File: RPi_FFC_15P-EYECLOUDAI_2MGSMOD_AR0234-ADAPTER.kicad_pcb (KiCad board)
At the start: 2 copper layers, 40.4 x 40.5 mm, 21 parts, among them J1 1-84952-5, J2 3-1734592-0, P1 53261-0371, P2 53261-0371, U1 MIC5259-1.8YD5-TR, U2 APX803-29SAG-7, X1 24MHz

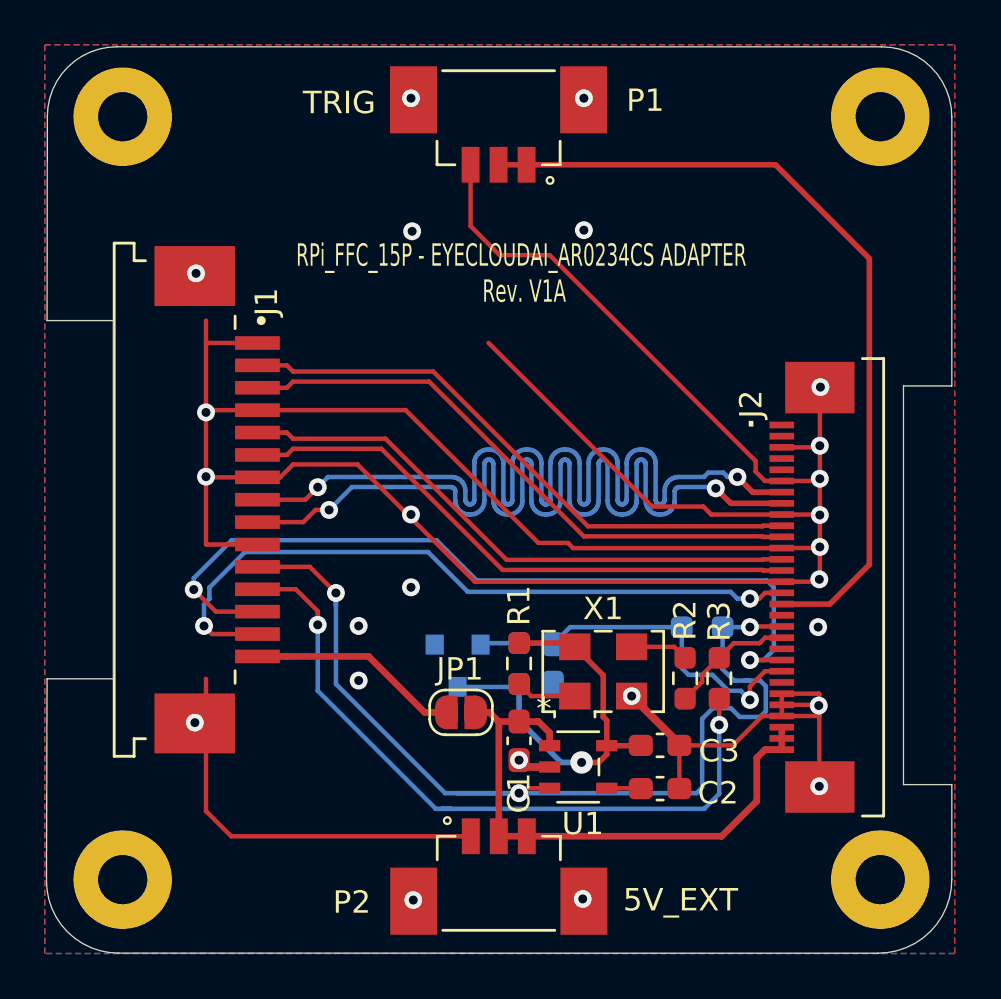
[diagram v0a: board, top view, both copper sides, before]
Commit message: Add level shifters for 3V3<->1V8 signals
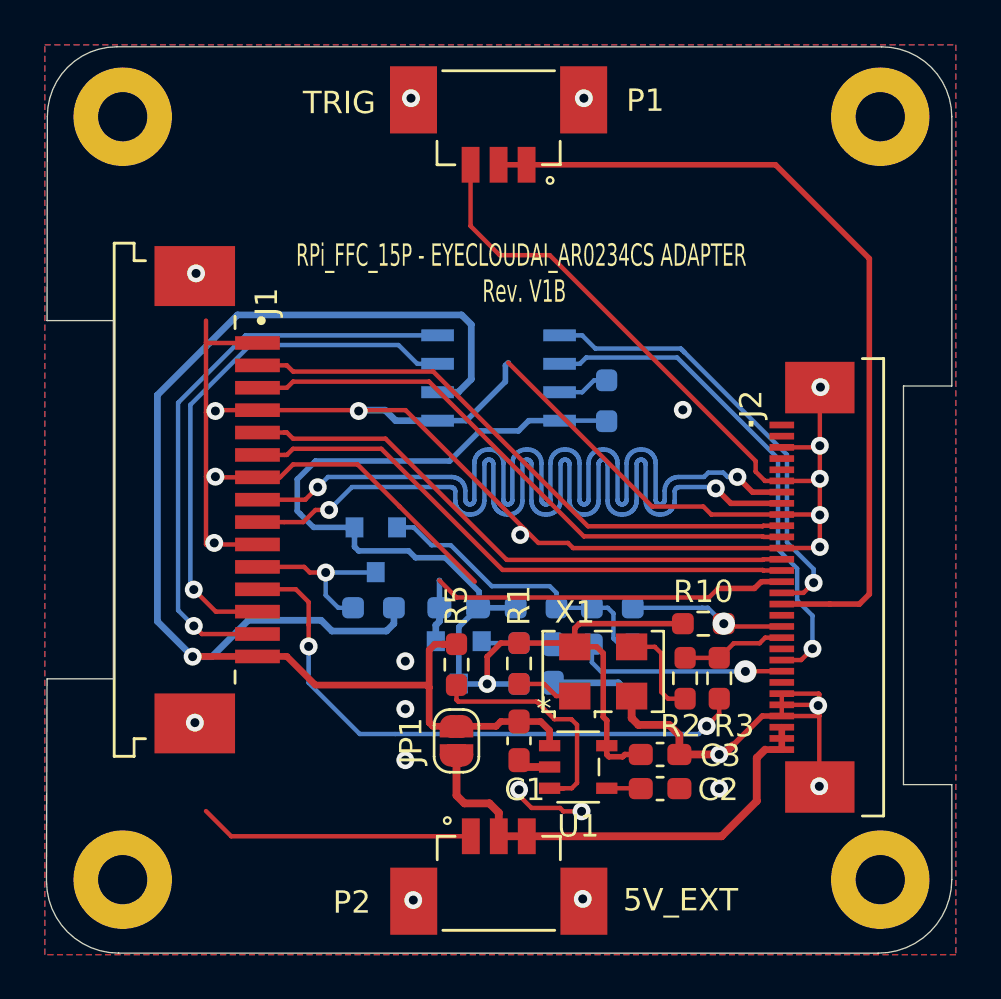
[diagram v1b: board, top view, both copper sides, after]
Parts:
- added C5: 0.01uF, Capacitor_SMD:C_0603_1608Metric_Pad1.08x0.95mm_HandSolder, B.Cu at (120.1, 101.3)
- added Q1: BSS138, Package_TO_SOT_SMD:SOT-23, B.Cu at (116.4, 98.8)
- added R10: 10K, Resistor_SMD:R_0603_1608Metric_Pad0.98x0.95mm_HandSolder, F.Cu at (131.0, 102.1)
- added R11: 10K, Resistor_SMD:R_0603_1608Metric_Pad0.98x0.95mm_HandSolder, B.Cu at (126.7, 92.1)
- added R6: 10K, Resistor_SMD:R_0603_1608Metric_Pad0.98x0.95mm_HandSolder, B.Cu at (116.3, 101.3)
- added R7: 10K, Resistor_SMD:R_0603_1608Metric_Pad0.98x0.95mm_HandSolder, B.Cu at (123.5, 101.3)
- added R8: 0, Resistor_SMD:R_0603_1608Metric_Pad0.98x0.95mm_HandSolder, B.Cu at (126.9, 101.3)
- added R9: 0, Resistor_SMD:R_0603_1608Metric_Pad0.98x0.95mm_HandSolder, B.Cu at (126.9, 103.0)
- added U3: PCA9306D, footprints:PCA9306D, B.Cu at (121.9, 91.1)
- R5: value 0 -> 10K; moved to F.Cu
- moved R5 11.1 mm to (120.0, 103.9), turned to 270 degrees
- moved JP1 1.29 mm to (120.0, 107.3), turned to 90 degrees
- moved C3 0.41 mm to (129.1, 107.9)
- moved U2 0.16 mm to (120.1, 103.8)
- turned R2 to 270 degrees
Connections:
- net Net-(J1-Pad12) renamed /MCLK_JETSON
- net Net-(R2-Pad2) renamed /MCLK_OSC
- C1 pad 1: +5V -> +3V3
- J1 pad 11: /CSI_PWDN_1V8 -> /CSI_GPIO_3V3
- J1 pad 13: /I2C_SCL_1V8 -> /I2C_SCL_3V3
- J1 pad 14: /I2C_SDA_1V8 -> /I2C_SDA_3V3
- R5 pad 1: /CSI_nRST_1V8 -> +3V3
- R5 pad 2: /CSI_PWDN_1V8 -> Net-(R5-Pad2)
- U1 pad 1: +5V -> +3V3
- U1 pad 3: /CSI_PWDN_1V8 -> Net-(R5-Pad2)
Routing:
- net +3V3: track 9.48 -> 66.8 mm, vias 0 -> 1
- net /CSI_PWDN_1V8: track 45.5 -> 7.44 mm, vias 3 -> 1
- net +1V8: track 19.1 -> 54.1 mm
- net /I2C_SDA_3V3: track 0.00 -> 26.1 mm, vias 0 -> 1
- net /I2C_SCL_3V3: track 0.00 -> 24.1 mm, vias 0 -> 1
- net /I2C_SCL_1V8: track 36.7 -> 22.5 mm, vias 2 -> 1
- net Net-(Q1-Pad2): track 0.00 -> 13.7 mm
- net /I2C_SDA_1V8: track 31.5 -> 20.4 mm, vias 2 -> 1
- net Net-(R5-Pad2): track 0.00 -> 11.1 mm
- net GND: track 165.7 -> 175.5 mm, vias 25 -> 26
- net /CSI_GPIO_3V3: track 0.00 -> 7.86 mm, vias 0 -> 1
- net /MCLK_JETSON: track 31.7 -> 26.5 mm
- net +5V: track 25.8 -> 21.4 mm
- net /CSI_nRST_1V8: track 17.1 -> 14.5 mm
- net Net-(R11-Pad2): track 0.00 -> 2.32 mm
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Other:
- board text added: "RPi_FFC_15P - EYECLOUDAI_AR0234CS ADAPTER Rev. V1B"
- board text removed: "RPi_FFC_15P - EYECLOUDAI_AR0234CS ADAPTER Rev. V1A"

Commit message: Add V1C
	Add 15pF capacitor at the ouput pin of the oscillator.
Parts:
- removed the R2 at (130.2, 104.5)
- added C4: 15pF, Capacitor_SMD:C_0603_1608Metric_Pad1.08x0.95mm_HandSolder, F.Cu at (130.1, 104.5)
- renumbered C4 to C6, R11 to R10, R10 to R2
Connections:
- P1 pad P1: GND -> (no net)
- P1 pad P2: GND -> (no net)
- P2 pad P1: GND -> (no net)
- P2 pad P2: GND -> (no net)
- X1 pad 3: /MCLK_OSC -> /CSI_MCLK_1V8
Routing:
- net /MCLK_OSC: track 4.36 -> 0.00 mm
- net GND: track 175.5 -> 178.5 mm, vias 26 -> 22
- net /CSI_MCLK_1V8: track 4.98 -> 7.61 mm
- net (no net): vias 0 -> 4
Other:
- board text added: "RPi_FFC_15P - EYECLOUDAI_AR0234CS ADAPTER Rev. V1C"
- board text removed: "RPi_FFC_15P - EYECLOUDAI_AR0234CS ADAPTER Rev. V1B"
